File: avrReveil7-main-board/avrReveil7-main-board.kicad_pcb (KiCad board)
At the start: 2 copper layers, 0 parts

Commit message: schematic ok, started pcb (unfinished)
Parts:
- added BT1: coin cell 2032, Battery:Battery_Panasonic_CR2032-HFN_Horizontal_CircularHoles, F.Cu at (159.5, 69.7)
- added C1: 22pF, Capacitor_THT:C_Disc_D3.4mm_W2.1mm_P2.50mm, F.Cu at (122.9, 137.5)
- added C2: 22pF, Capacitor_THT:C_Disc_D3.4mm_W2.1mm_P2.50mm, F.Cu at (102.1, 137.5)
- added C3: 22pF, Capacitor_THT:C_Disc_D3.4mm_W2.1mm_P2.50mm, F.Cu at (91.5, 94.0)
- added C4: 22pF, Capacitor_THT:C_Disc_D3.4mm_W2.1mm_P2.50mm, F.Cu at (91.5, 98.8)
- added C5: C, Capacitor_THT:C_Disc_D3.4mm_W2.1mm_P2.50mm, F.Cu at (114.5, 92.8)
- added C6: C_Polarized, Capacitor_THT:CP_Radial_D6.3mm_P2.50mm, F.Cu at (83.5, 129.0)
- added D1: D, Diode_THT:D_T-1_P5.08mm_Horizontal, F.Cu at (150.0, 97.5)
- added J1: AVR-ISP-6, Connector_IDC:IDC-Header_2x03_P2.54mm_Vertical, F.Cu at (78.0, 82.6)
- added J_FRONT1: Front connector, Connector_PinSocket_2.54mm:PinSocket_1x04_P2.54mm_Vertical, F.Cu at (82.2, 64.5)
- added J_PORTC1: Conn_01x03, Connector_PinHeader_2.54mm:PinHeader_1x03_P2.54mm_Vertical, F.Cu at (118.5, 85.0)
- added J_USB1: Conn_01x04, Connector_PinHeader_2.54mm:PinHeader_1x04_P2.54mm_Vertical, F.Cu at (91.5, 126.7)
- added M1: Motor_DC, Connector_PinHeader_2.54mm:PinHeader_1x02_P2.54mm_Vertical, F.Cu at (168.5, 100.5)
- added Q1: 2N5551, Package_TO_SOT_THT:TO-92L_Inline, F.Cu at (157.4, 106.7)
- added R1: 100, Resistor_THT:R_Axial_DIN0207_L6.3mm_D2.5mm_P10.16mm_Horizontal, F.Cu at (152.1, 122.0)
- added R2: R, Resistor_THT:R_Axial_DIN0207_L6.3mm_D2.5mm_P2.54mm_Vertical, F.Cu at (146.5, 105.5)
- added R3: 10k, Resistor_THT:R_Axial_DIN0204_L3.6mm_D1.6mm_P1.90mm_Vertical, F.Cu at (124.0, 69.6)
- added R4: 10k, Resistor_THT:R_Axial_DIN0204_L3.6mm_D1.6mm_P1.90mm_Vertical, F.Cu at (124.0, 79.4)
- added SW1: SW_Push, Connector_PinHeader_2.54mm:PinHeader_1x02_P2.54mm_Vertical, F.Cu at (87.0, 109.0)
- added SW2: SW_Push, Connector_PinHeader_2.54mm:PinHeader_1x02_P2.54mm_Vertical, F.Cu at (87.3, 115.0)
- added U1: CH340G, Package_SO:SOIC-16_3.9x9.9mm_P1.27mm, B.Cu at (114.0, 122.5)
- added U2: ATmega328-P, Package_DIP:DIP-28_W7.62mm, F.Cu at (102.0, 74.9)
- added U3: TCRT5000, Vishay tcrt5000:tcrt5000, F.Cu at (147.0, 130.0)
- added U4: DS3231M, Package_SO:SOIC-16W_7.5x10.3mm_P1.27mm, B.Cu at (136.5, 78.5)
- added Y1: 12MHz, Crystal:Crystal_HC18-U_Vertical, F.Cu at (110.2, 137.5)
- added Y2: 20MHz, Crystal:Crystal_HC18-U_Vertical, F.Cu at (86.0, 99.0)
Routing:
- net GND: track 0.00 -> 353.3 mm, vias 0 -> 2
- net VCC: track 0.00 -> 313.0 mm, vias 0 -> 4
- net Net-(U1-RXD): track 0.00 -> 75.6 mm, vias 0 -> 2
- net Net-(U1-TXD): track 0.00 -> 72.1 mm, vias 0 -> 2
- net Net-(BT1-+): track 0.00 -> 48.9 mm, vias 0 -> 4
- net Net-(J_USB1-Pin_3): track 0.00 -> 31.0 mm, vias 0 -> 2
- net Net-(J_USB1-Pin_2): track 0.00 -> 26.7 mm, vias 0 -> 2
- net /RTC_SDA: track 0.00 -> 25.3 mm
- net /RTC_SCL: track 0.00 -> 25.1 mm
- net //RST: track 0.00 -> 25.1 mm
- net /BTN2: track 0.00 -> 20.8 mm
- net Net-(U1-XI): track 0.00 -> 19.6 mm
- net /BTN1: track 0.00 -> 18.6 mm
- net Net-(U1-XO): track 0.00 -> 18.4 mm
- net Net-(U2-XTAL1/PB6): track 0.00 -> 16.5 mm
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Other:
- board outline added: 111.5 x 86.5 mm

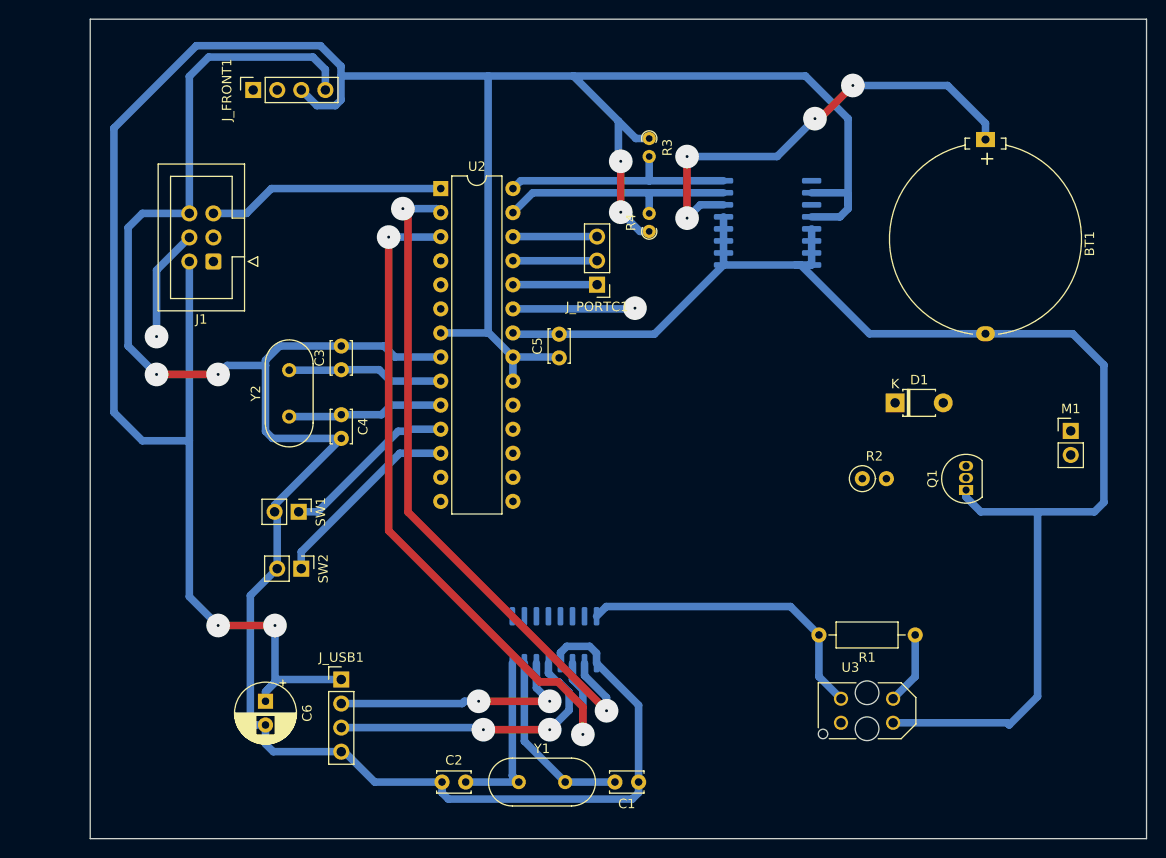
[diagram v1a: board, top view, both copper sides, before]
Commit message: PCB draft completed, to be tested separately before sent to prod at home
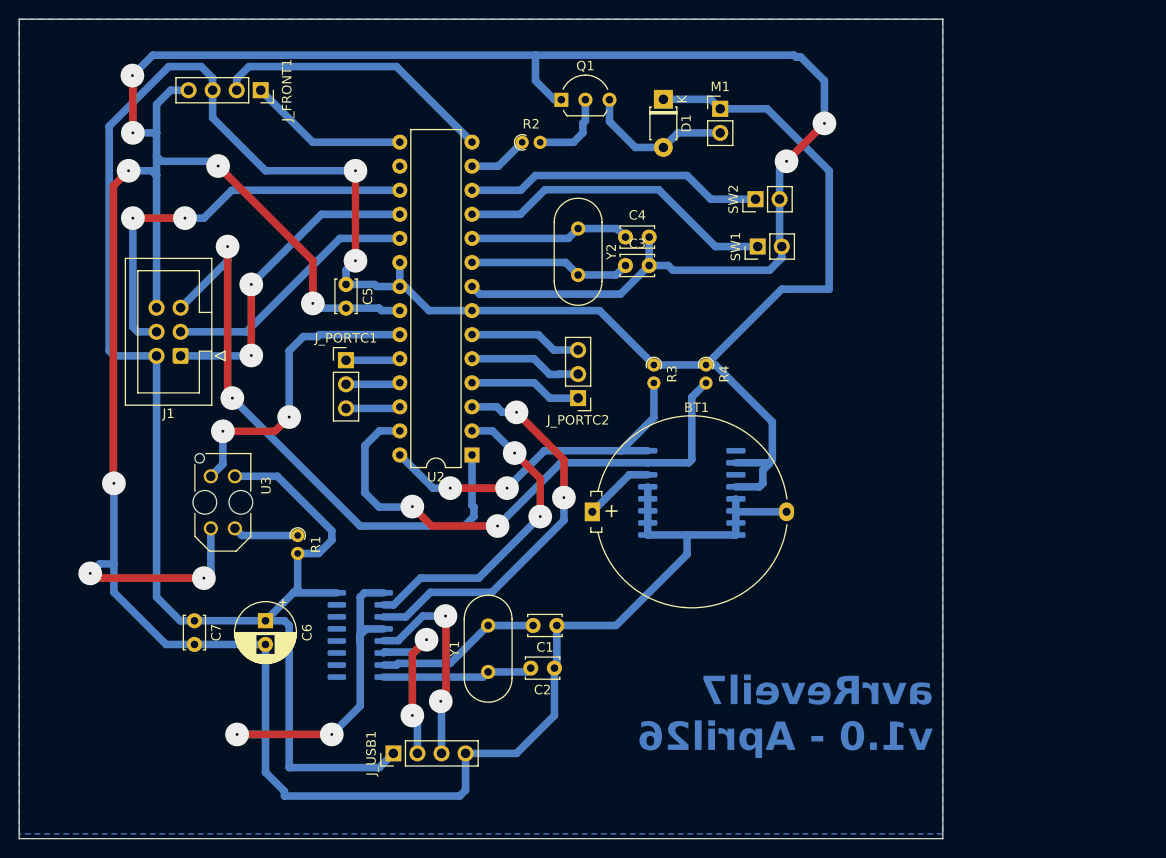
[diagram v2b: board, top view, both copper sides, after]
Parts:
- added C7: C, Capacitor_THT:C_Disc_D3.4mm_W2.1mm_P2.50mm, F.Cu at (76.0, 120.5)
- added J_PORTC2: Conn_01x03, Connector_PinHeader_2.54mm:PinHeader_1x03_P2.54mm_Vertical, F.Cu at (116.5, 97.0)
- Q1: footprint Package_TO_SOT_THT:TO-92L_Inline -> Package_TO_SOT_THT:TO-92L_Inline_Wide
- R1: footprint Resistor_THT:R_Axial_DIN0207_L6.3mm_D2.5mm_P10.16mm_Horizontal -> Resistor_THT:R_Axial_DIN0204_L3.6mm_D1.6mm_P1.90mm_Vertical
- R2: footprint Resistor_THT:R_Axial_DIN0207_L6.3mm_D2.5mm_P2.54mm_Vertical -> Resistor_THT:R_Axial_DIN0204_L3.6mm_D1.6mm_P1.90mm_Vertical
- moved U3 71.5 mm to (79.0, 108.0), turned to -90 degrees
- moved R1 66.0 mm to (86.9, 111.5), turned to -90 degrees
- moved SW2 61.8 mm to (135.2, 76.0), turned to 90 degrees
- moved Q1 59.4 mm to (114.7, 65.5), turned to 0 degrees
- moved BT1 57.2 mm to (118.0, 109.0), turned to 0 degrees
- moved SW1 56.0 mm to (135.5, 81.0), turned to 90 degrees
- moved R2 50.5 mm to (110.6, 70.0)
- moved M1 50.2 mm to (131.5, 66.5)
- moved D1 40.3 mm to (125.5, 65.5), turned to -90 degrees
- moved Y2 36.4 mm to (116.5, 79.1), turned to -90 degrees
- moved C4 35.4 mm to (121.5, 80.0), turned to 0 degrees
- moved C3 32.0 mm to (121.5, 83.0), turned to 0 degrees
- moved U4 29.6 mm to (128.5, 107.0)
- moved U2 28.3 mm to (105.3, 103.0), turned to 180 degrees
- moved J_PORTC1 27.7 mm to (92.0, 93.0), turned to 0 degrees
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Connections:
- U2 pad 4: unconnected-(U2-PD2-Pad4) -> Net-(J_PORTC2-Pin_1)
- U2 pad 5: unconnected-(U2-PD3-Pad5) -> Net-(J_PORTC2-Pin_2)
- U2 pad 6: unconnected-(U2-PD4-Pad6) -> Net-(J_PORTC2-Pin_3)
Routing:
- net GND: track 353.3 -> 434.6 mm, vias 2 -> 12
- net Net-(BT1-+): track 48.9 -> 7.47 mm, vias 4 -> 0
- net Net-(U1-TXD): track 72.1 -> 33.7 mm
- net //RST: track 25.1 -> 62.8 mm, vias 0 -> 2
- net Net-(U1-RXD): track 75.6 -> 41.7 mm
- net /ISP_MISO: track 0.00 -> 33.7 mm, vias 0 -> 2
- net /ISP_MOSI: track 11.9 -> 43.6 mm, vias 1 -> 2
- net /RTC_SDA: track 25.3 -> 56.9 mm, vias 0 -> 2
- net Net-(J_FRONT1-Pin_2): track 0.00 -> 29.9 mm
- net /ISP_CLK: track 0.00 -> 27.2 mm
- net VCC: track 313.0 -> 291.6 mm, vias 4 -> 2
- net /PROX_OUT: track 12.9 -> 32.3 mm, vias 1 -> 2
- net Net-(J_FRONT1-Pin_1): track 0.00 -> 16.9 mm
- net Net-(D1-A): track 0.00 -> 15.8 mm
- net /BTN1: track 18.6 -> 33.7 mm
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- added copper zone on B.Cu, net (none)
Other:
- board size 111.5 x 86.5 mm -> 97.5 x 86.5 mm
- board text added: "avrReveil7 v1.0 - April26"
